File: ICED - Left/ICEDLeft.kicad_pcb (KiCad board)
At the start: 2 copper layers, 175.3 x 145 mm, 164 parts, among them P1 FLASH_HDR, P2 USBC, P3 CONN_17, P4 USB3_AFEMALE, Q1 TC1264, U1 MK20DX256VLH7, U2 IS31FL3731C, X1 CRYSTAL

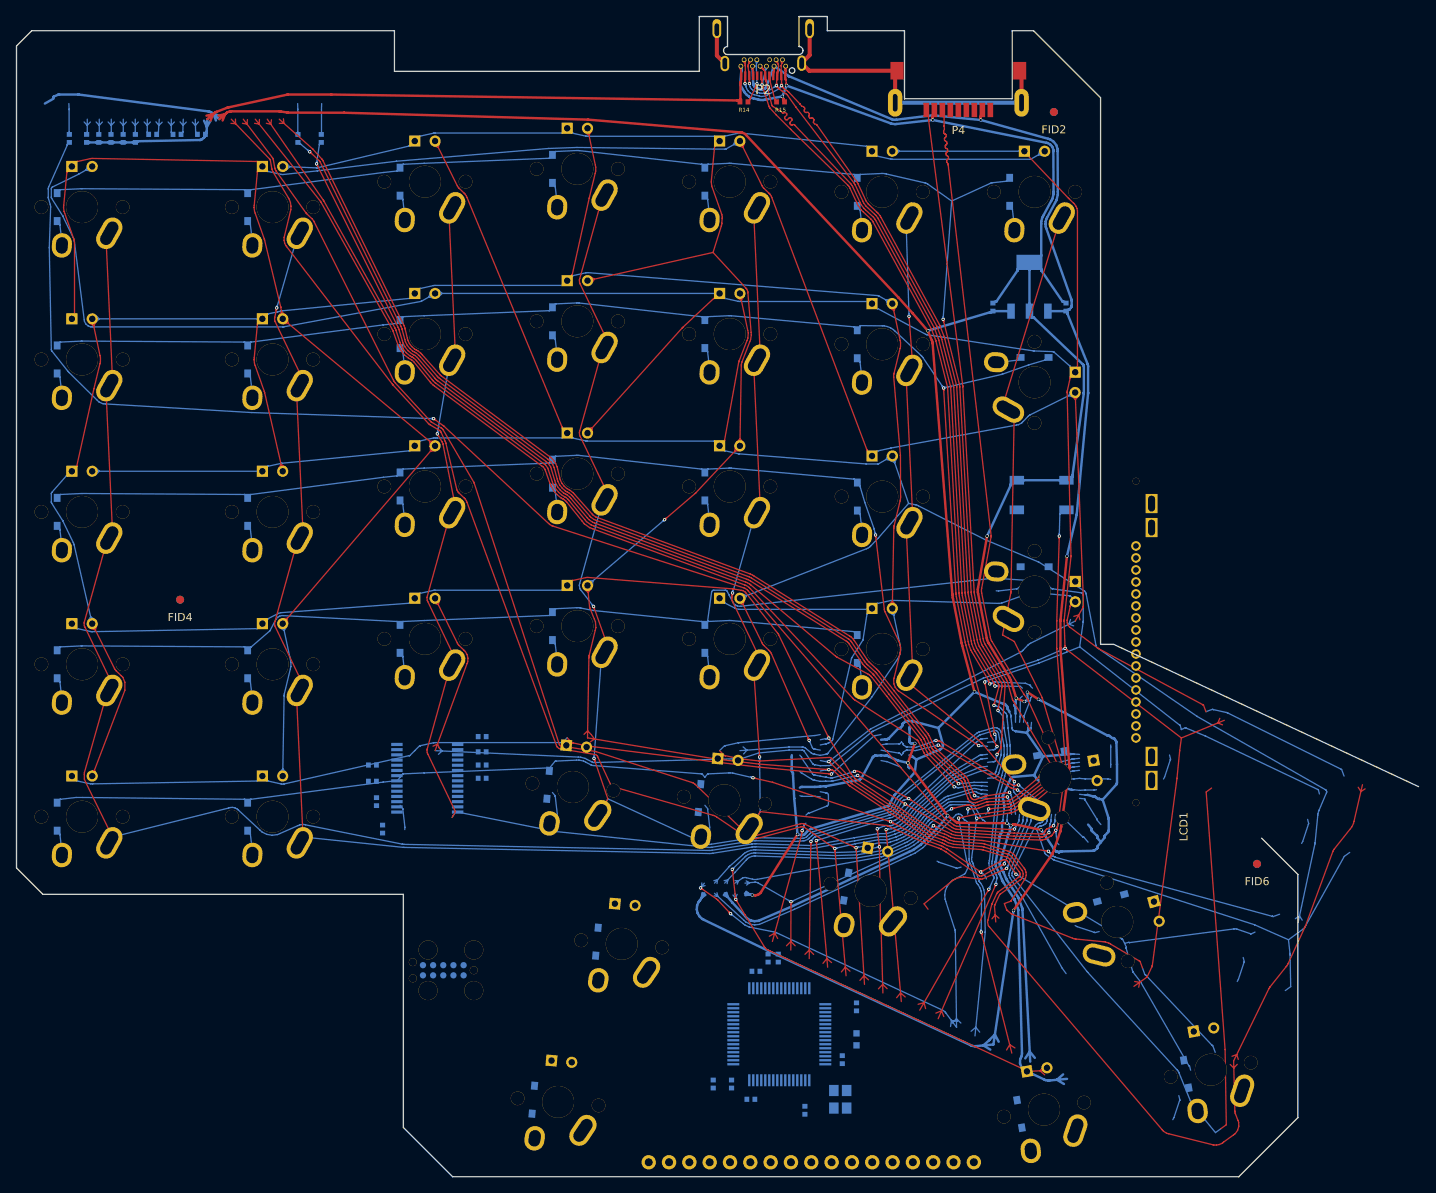
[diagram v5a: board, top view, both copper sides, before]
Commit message: more cut line moves
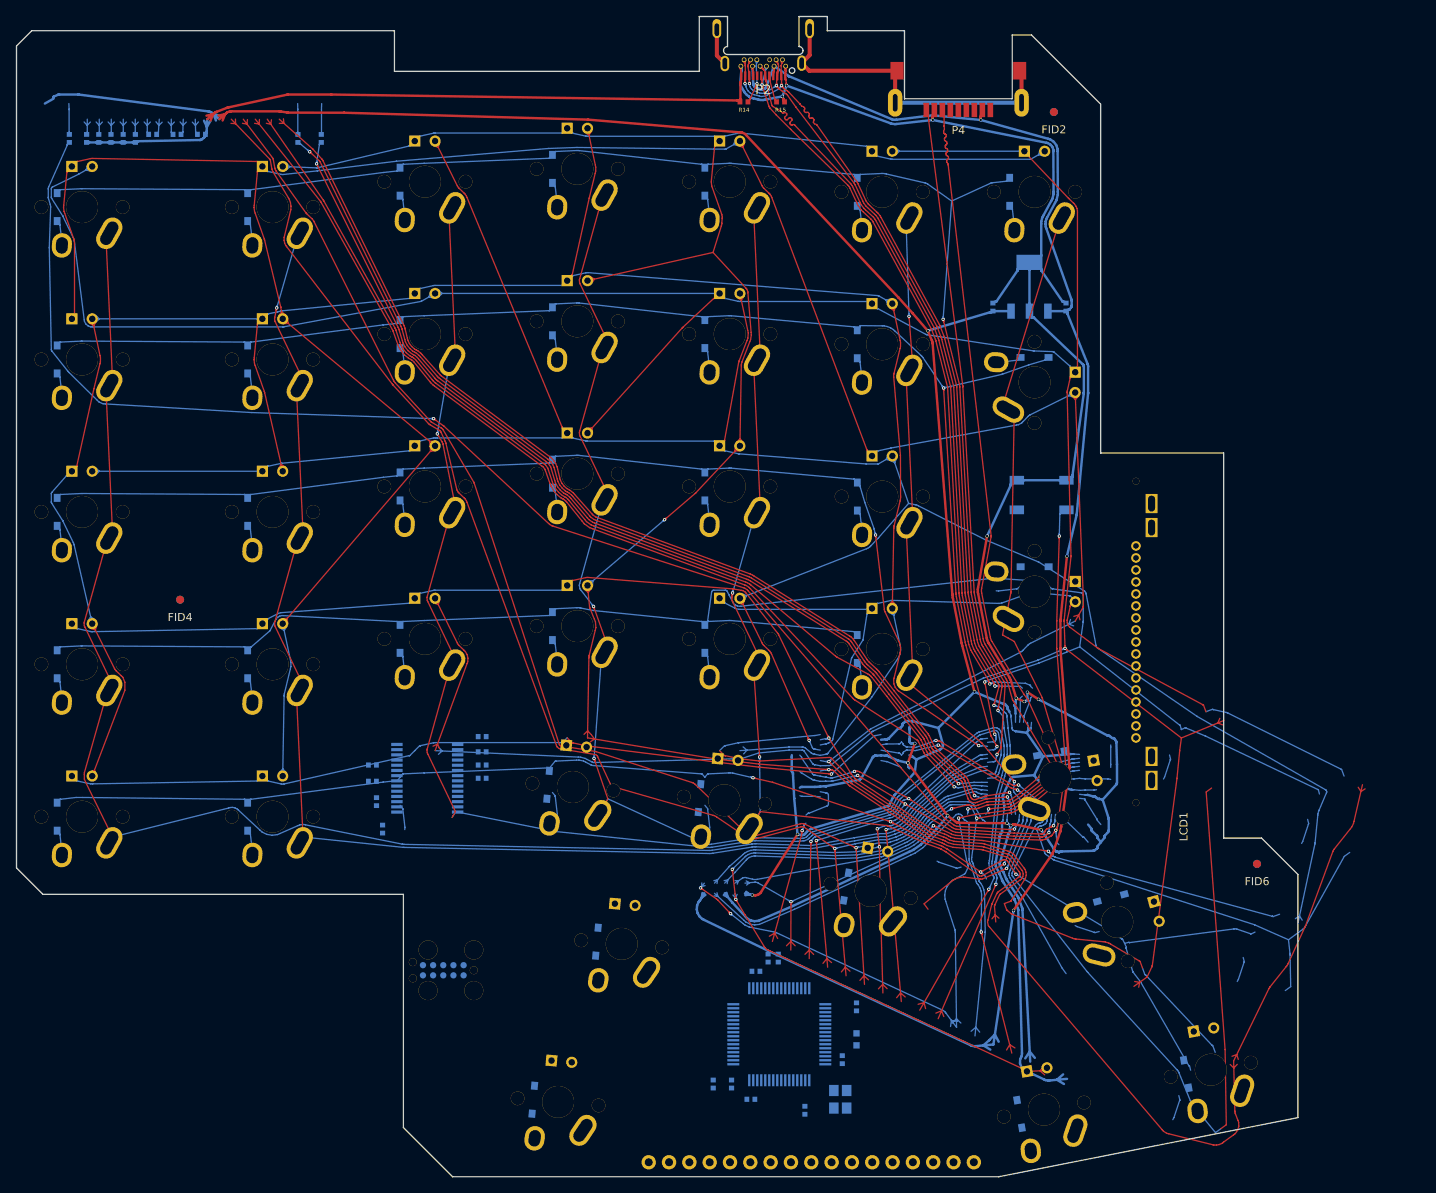
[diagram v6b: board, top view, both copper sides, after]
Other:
- board size 175.3 x 145 mm -> 160.2 x 145 mm
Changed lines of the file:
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@@
     (effects (font (size 2.032 1.524) (thickness 0.3048)) (justify left mirror))
   )
-  (gr_line (start 153.162 35.941) (end 144.78 27.559) (angle 90) (layer Edge.Cuts) (width 0.127))
-  (gr_line (start 153.162 104.267) (end 154.813 104.267) (angle 90) (layer Edge.Cuts) (width 0.127))
-  (gr_line (start 153.162 35.941) (end 153.162 104.267) (angle 90) (layer Edge.Cuts) (width 0.127))
+  (gr_line (start 153.167 36.73) (end 144.533 28.097) (angle 90) (layer Edge.Cuts) (width 0.127))
+  (gr_line (start 168.546 80.344) (end 153.167 80.344) (angle 90) (layer Edge.Cuts) (width 0.127))
+  (gr_line (start 153.167 80.344) (end 153.167 36.73) (angle 90) (layer Edge.Cuts) (width 0.127))
   (gr_line (start 17.653 29.464) (end 19.558 27.559) (angle 90) (layer Edge.Cuts) (width 0.127))
   (gr_line (start 17.653 132.207) (end 20.955 135.509) (angle 90) (layer Edge.Cuts) (width 0.127))
   (gr_line (start 17.653 29.464) (end 17.653 132.207) (angle 90) (layer Edge.Cuts) (width 0.127))
+  (gr_line (start 173.279 128.477) (end 168.546 128.477) (angle 90) (layer Edge.Cuts) (width 0.127))
   (gr_line (start 177.828 133.026) (end 173.279 128.477) (angle 90) (layer Edge.Cuts) (width 0.127))
   (gr_line (start 177.828 163.422) (end 177.828 133.026) (angle 90) (layer Edge.Cuts) (width 0.127))
-  (gr_line (start 72.16929 170.815) (end 170.434 170.815) (angle 90) (layer Edge.Cuts) (width 0.127))
-  (gr_line (start 177.828 163.422) (end 170.434 170.815) (angle 90) (layer Edge.Cuts) (width 0.127))
-  (gr_line (start 66.012873 135.509) (end 66.012873 164.658583) (angle 90) (layer Edge.Cuts) (width 0.127))
-  (gr_line (start 66.012873 164.658583) (end 72.16929 170.815) (angle 90) (layer Edge.Cuts) (width 0.127))
-  (gr_line (start 192.913 122.047) (end 154.813 104.267) (angle 90) (layer Edge.Cuts) (width 0.127))
-  (gr_line (start 66.012873 135.509) (end 20.955 135.509) (angle 90) (layer Edge.Cuts) (width 0.127))
+  (gr_line (start 72.16929 170.815) (end 140.41 170.815) (angle 90) (layer Edge.Cuts) (width 0.127))
+  (gr_line (start 177.828 163.422) (end 140.41 170.815) (angle 90) (layer Edge.Cuts) (width 0.127))
+  (gr_line (start 66.013 135.509) (end 66.013 164.659) (angle 90) (layer Edge.Cuts) (width 0.127))
+  (gr_line (start 66.013 164.659) (end 72.16929 170.815) (angle 90) (layer Edge.Cuts) (width 0.127))
+  (gr_line (start 168.546 128.477) (end 168.546 80.344) (angle 90) (layer Edge.Cuts) (width 0.127))
+  (gr_line (start 66.013 135.509) (end 20.955 135.509) (angle 90) (layer Edge.Cuts) (width 0.127))
   (gr_line (start 64.897 27.559) (end 19.558 27.559) (angle 90) (layer Edge.Cuts) (width 0.127))
   (gr_line (start 64.897 32.639) (end 64.897 27.559) (angle 90) (layer Edge.Cuts) (width 0.127))
@@
   (gr_line (start 128.651 36.068) (end 128.651 27.559) (angle 90) (layer Edge.Cuts) (width 0.127))
   (gr_line (start 142.113 36.068) (end 128.651 36.068) (angle 90) (layer Edge.Cuts) (width 0.127))
-  (gr_line (start 142.113 27.559) (end 142.113 36.068) (angle 90) (layer Edge.Cuts) (width 0.127))
-  (gr_line (start 144.78 27.559) (end 142.113 27.559) (angle 90) (layer Edge.Cuts) (width 0.127))
+  (gr_line (start 142.113 28.097) (end 142.113 36.068) (angle 90) (layer Edge.Cuts) (width 0.127))
+  (gr_line (start 144.533 28.097) (end 142.113 28.097) (angle 90) (layer Edge.Cuts) (width 0.127))
   (gr_text SCL0 (at 101.76 167.4 270) (layer B.SilkS)
     (effects (font (size 2.032 1.524) (thickness 0.3048)) (justify left mirror))
